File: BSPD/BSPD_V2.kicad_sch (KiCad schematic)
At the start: 36 parts, among them J2 Conn_01x02_Socket, J3 Conn_01x02_Socket, J4 Conn_01x02_Socket, K1 Fujitsu_FTR-LYCA005x, Q1 AO3400A, Q2 AO3400A, Q3 NPN, Q4 AO3400A, Q5 NPN, U1 CD4001BM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

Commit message: Some QoL changes like 500 ohms for the reset of the SR latch(don't really require a smaller one as if the car is switched off the capacitance/charge will dissipate in due time). Scratch that, emergency, even after 2-5mins , it barely reaches 11.98V. :(
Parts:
- R15, R21: value 1 -> 500
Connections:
- net GND: now also R21.1; no longer R21.2
- net Q_ouput: now also R15.2; no longer K1.A2, R21.1
- net at R3.1, U5.3 (+): now also R4.1; no longer R15.2
- net at R15.1: now also K1.A2, R21.2; no longer R4.1
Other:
- note added: "Anything below 250 is unfeasible, approx 1-2 W. Therefore using 500 ohm."
- note added: "Can increase the value of C for better supply fluctuation"
- note added: "Depends on Brake pressure range"
- note added: "Huge doubts regarding the CD series datasheets of digital gates. Ask seniors for clarifications."
- note added: "Just need to find a BJT for with suitable values"
- note added: "These divider values are for CS o/p values of 2.2V to 10.5V"
- note added: "Voltage divider for assurity that the A2 is lower than A1 for the relay to work properly always."
- moved on the sheet: R21, R4, U1, U2

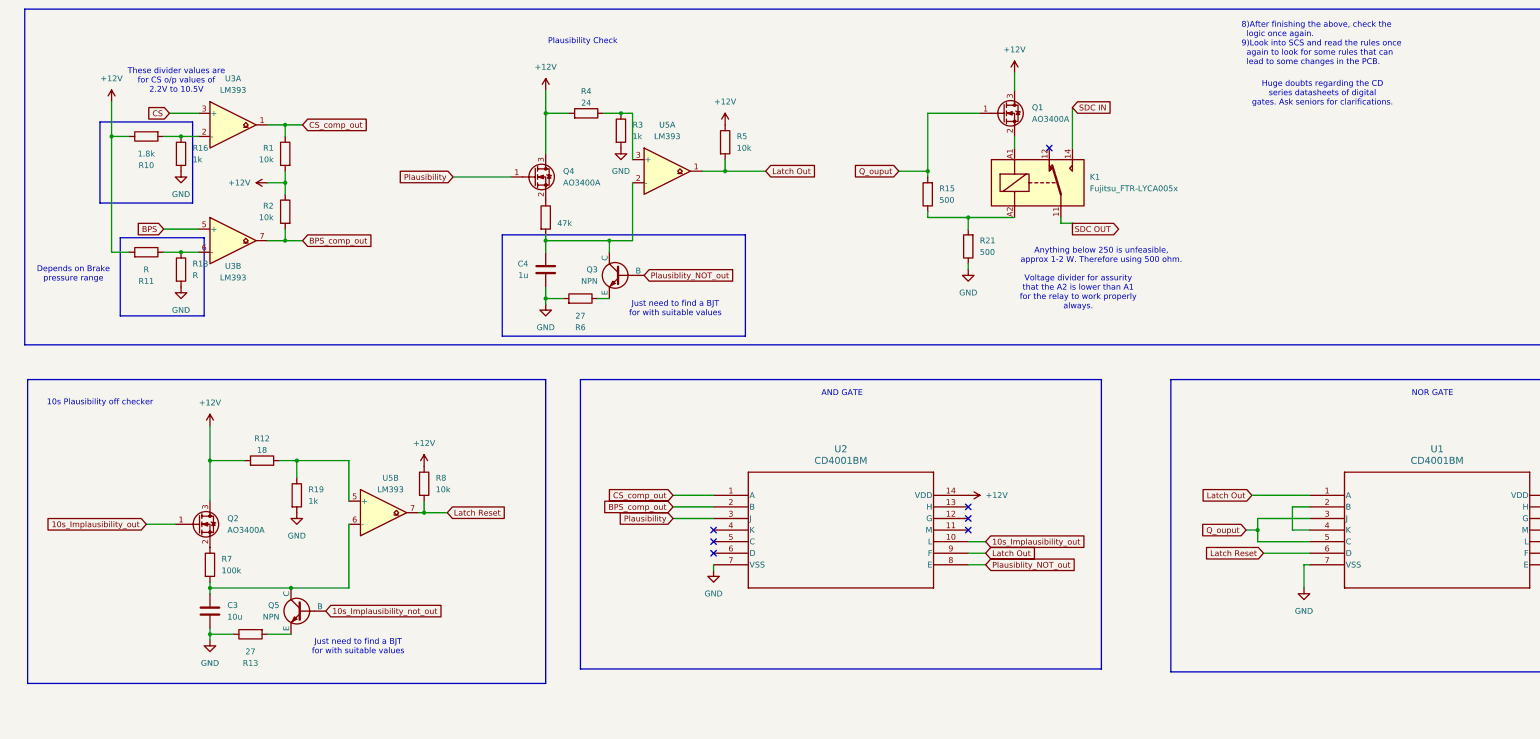
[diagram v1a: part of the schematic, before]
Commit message: Hysteris for comparators
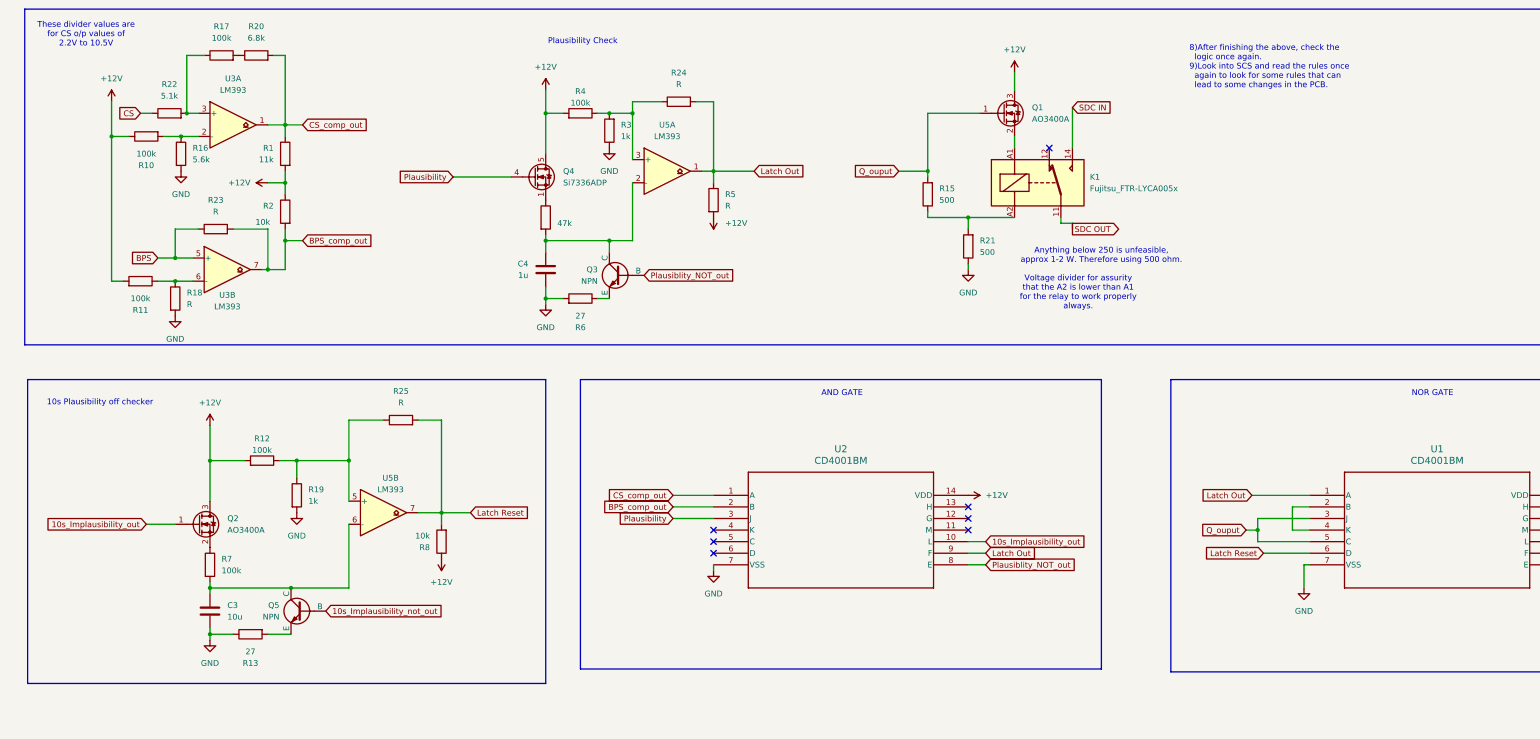
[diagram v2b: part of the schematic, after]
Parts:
- removed Q4: AO3400A, Package_TO_SOT_SMD:SOT-23, symbol Transistor_FET:AO3400A
- added Q4: Si7336ADP, Package_SO:PowerPAK_SO-8_Single, symbol Transistor_FET:Si7336ADP
- added R17: 100k, symbol Device:R
- added R20: 6.8k, symbol Device:R
- added R22: 5.1k, symbol Device:R
- added R23, R24, R25: R, symbol Device:R
- R1: value 10k -> 11k
- R10: value 1.8k -> 100k
- R11: value R -> 100k
- R12: value 18 -> 100k
- R16: value 1k -> 5.6k
- R4: value 24 -> 100k
- R5: value 10k -> R
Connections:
- net +12V: now also R5.2, Q4.5 (D); no longer R5.1
- net BPS: now also R23.1
- net BPS_comp_out: now also R23.2
- net CS: now also R22.1; no longer U3.3 (+)
- net CS_comp_out: now also R20.2
- net GND: now also R3.1; no longer R3.2
- net Latch Out: now also R5.1, R24.2; no longer R5.2
- net Latch Reset: now also R25.2
- net Plausibility: now also Q4.4 (G)
- net at R4.1, U5.3 (+): now also R3.2, R24.1; no longer R3.1
- net at R12.1, R19.1, U5.5 (+): now also R25.1
- net at R14.1: now also Q4.1 (S), Q4.2 (S), Q4.3 (S)
- new net: R17.1, R22.2, U3.3 (+)
- new net: R17.2, R20.1
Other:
- note removed: "Depends on Brake pressure range"
- note removed: "Huge doubts regarding the CD series datasheets of digital gates. Ask seniors for clarifications."
- note removed: "Just need to find a BJT for with suitable values"
- moved on the sheet: R11, R18, R3, R4, U3B
